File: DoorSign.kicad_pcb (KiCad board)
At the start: 2 copper layers, 37 parts, among them J1 Wall, J2 Taster, J3 Taster-LED, U1 Pico, U2 PC817, U3 LM2575-5.0BT

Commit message: Ignores
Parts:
- C1, C10: footprint Capacitor_THT:CP_Axial_L11.0mm_D8.0mm_P15.00mm_Horizontal -> Capacitor_THT:CP_Radial_D12.5mm_P5.00mm
- C3, C5, D3, D5: moved to B.Cu
- C6, C8, D6, D8: moved to F.Cu
- moved D8 183.1 mm to (50.5, 155.4)
- moved C8 166.6 mm to (60.1, 155.9), turned to -90 degrees
- moved C9 154.6 mm to (59.0, 141.6)
- moved D9 154.6 mm to (68.0, 141.0)
- moved D6 135.1 mm to (174.3, 166.4), turned to 0 degrees
- moved C6 134.6 mm to (164.0, 166.0)
- moved J1 121.1 mm to (162.0, 112.7)
- moved C10 115.9 mm to (182.0, 90.7)
- moved C2 113.5 mm to (56.5, 36.4)
- moved D2 113.5 mm to (65.0, 37.0)
- moved D3 113.4 mm to (65.5, 48.6), turned to 180 degrees
- moved C3 113.2 mm to (57.0, 49.0)
- moved D7 112.1 mm to (154.8, 149.0), turned to 90 degrees
- moved D12 104.6 mm to (161.9, 99.1)
- moved D13 104.6 mm to (154.7, 114.1)
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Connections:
- U1 pad 1: unconnected-(U1-Pad1) -> Net-(R4-Pad2)
- U1 pad 2: unconnected-(U1-Pad2) -> Net-(D2-Pad4)
- U1 pad 21: Net-(R4-Pad2) -> unconnected-(U1-Pad21)
- U1 pad 22: Net-(D2-Pad4) -> unconnected-(U1-Pad22)
- U1 pad 29: Net-(R1-Pad2) -> unconnected-(U1-Pad29)
- U1 pad 31: unconnected-(U1-Pad31) -> Net-(R1-Pad2)
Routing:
- net Net-(D7-Pad2): track 19.4 -> 167.5 mm, vias 0 -> 1
- net /8VAC-L: track 138.4 -> 268.8 mm
- net Net-(D3-Pad2): track 17.9 -> 141.9 mm, vias 0 -> 1
- net Net-(J1-Pad3): track 128.2 -> 229.9 mm, vias 0 -> 2
- net +3.3V: track 98.2 -> 198.1 mm
- net Net-(D2-Pad4): track 163.4 -> 80.0 mm, vias 0 -> 2
- net Net-(R1-Pad2): track 87.0 -> 161.5 mm
- net Net-(D6-Pad2): track 15.7 -> 56.7 mm, vias 0 -> 1
- net Net-(J3-Pad2): track 14.3 -> 47.9 mm
- net Net-(R4-Pad2): track 47.6 -> 76.6 mm
- net /8VAC-N: track 47.6 -> 24.6 mm
- net Net-(C10-Pad1): track 47.6 -> 30.7 mm
- net Net-(D8-Pad2): track 16.8 -> 28.6 mm, vias 0 -> 1
- net Net-(D10-Pad1): track 26.8 -> 16.7 mm
- net Net-(D11-Pad1): track 38.9 -> 29.0 mm
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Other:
- board outline added: 179.8 x 179.8 mm

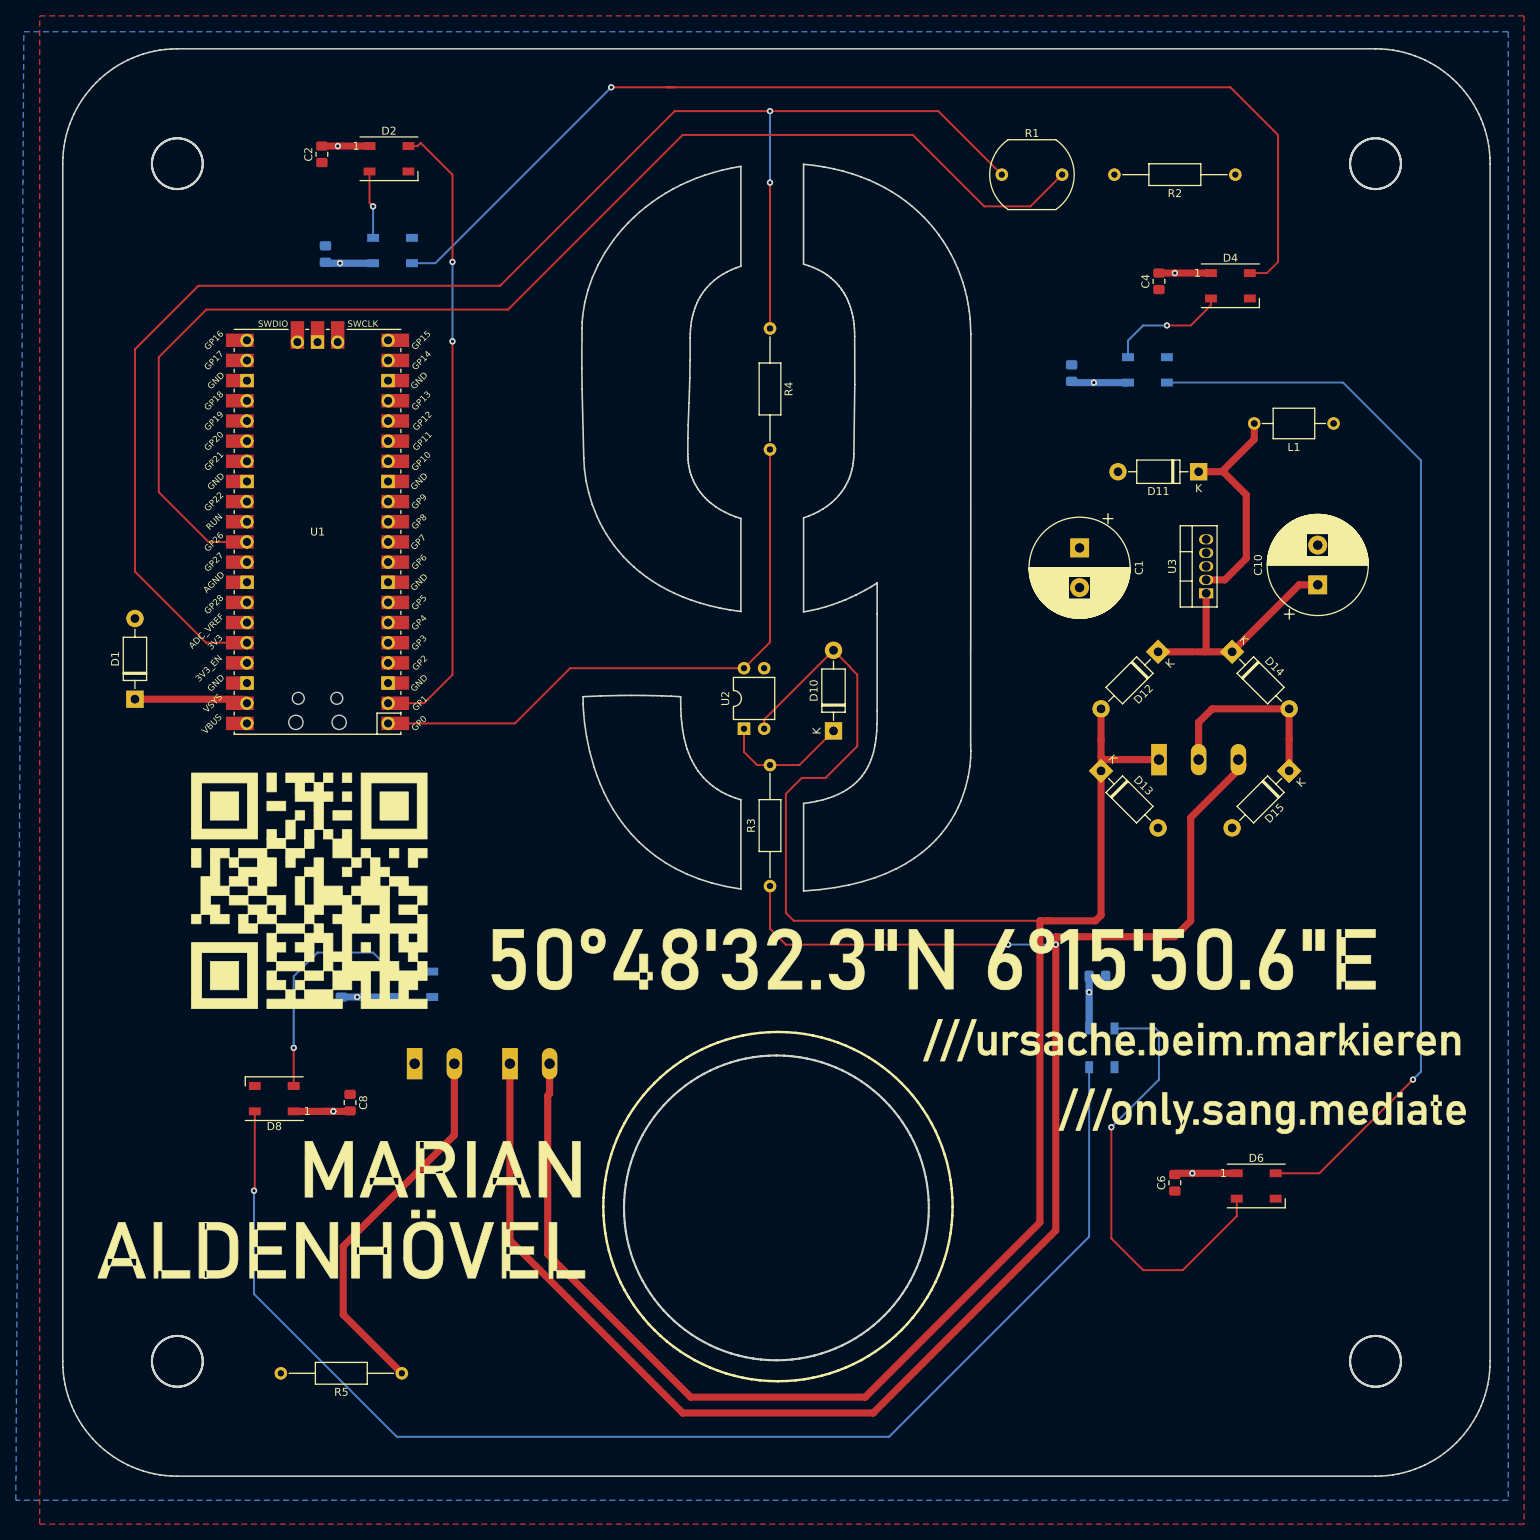
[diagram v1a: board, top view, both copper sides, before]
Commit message: Added BOM and partial schematics
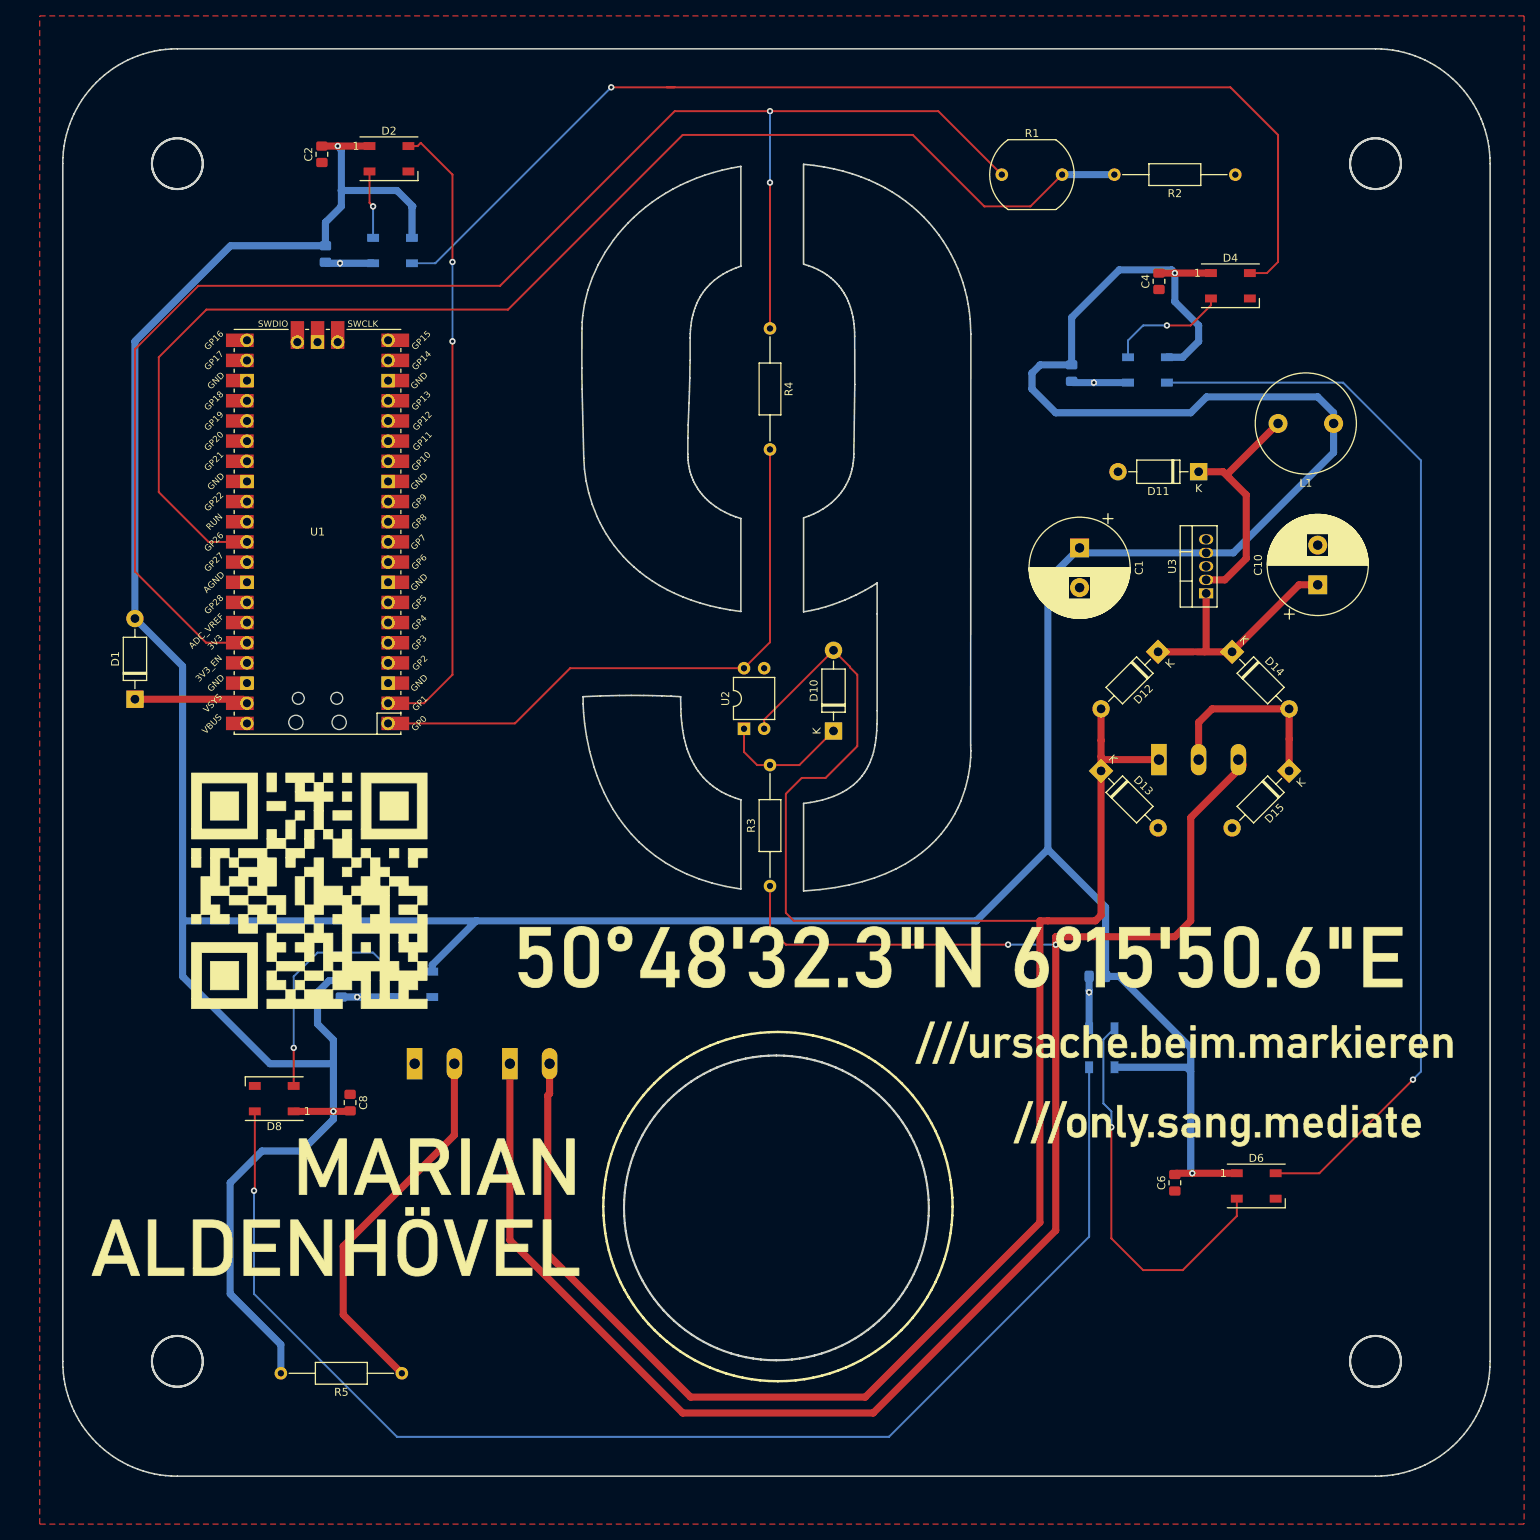
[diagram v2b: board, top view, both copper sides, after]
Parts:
- L1: value L -> 33uH; footprint Inductor_THT:L_Axial_L5.0mm_D3.6mm_P10.00mm_Horizontal_Murata_BL01RN1A2A2 -> Inductor_THT:L_Radial_D12.5mm_P7.00mm_Fastron_09HCP
- R2: value 100k -> 10k
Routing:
- net +5V: track 28.5 -> 600.7 mm
- net Net-(D6-Pad2): track 56.7 -> 49.9 mm
- net Net-(R1-Pad2): track 161.5 -> 168.1 mm
- net Net-(D11-Pad1): track 29.0 -> 30.8 mm
- removed copper zone on B.Cu, net +5V
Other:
- board text added: "<-- +5VDC Button Lamp"
- board text added: "<-- 8VAC L"
- board text added: "<-- 8VAC N"
- board text added: "<-- Button"
- board text added: "<-- GND Button Lamp"
- board text added: "<-- Ringer"

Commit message: added jumper for optocoupler
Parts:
- added JP4: Test, TestPoint:TestPoint_2Pads_Pitch2.54mm_Drill0.8mm, B.Cu at (97.0, 97.0)
- moved D1 5.53 mm to (35.0, 99.9), turned to -90 degrees
- moved C1 4.65 mm to (152.0, 90.7), turned to 90 degrees
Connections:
- C1 pad 1: +5V -> Net-(C1-Pad1)
- D1 pad 1: Net-(D1-Pad1) -> +5V
- D1 pad 2: +5V -> Net-(C1-Pad1)
- L1 pad 1: +5V -> Net-(C1-Pad1)
- U1 pad 39: Net-(D1-Pad1) -> +5V
- U3 pad 4: +5V -> Net-(C1-Pad1)
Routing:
- net Net-(C1-Pad1): track 0.00 -> 197.3 mm
- net Net-(D1-Pad1): track 14.3 -> 0.00 mm
- net +5V: track 600.7 -> 611.3 mm
- net Net-(JP4-Pad1): track 76.6 -> 80.9 mm
- net Net-(D5-Pad2): track 136.7 -> 138.4 mm

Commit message: connected all GND pins on the Pico
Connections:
- U1 pad 13: unconnected-(U1-Pad13) -> GND
- U1 pad 18: unconnected-(U1-Pad18) -> GND
- U1 pad 23: unconnected-(U1-Pad23) -> GND
- U1 pad 28: unconnected-(U1-Pad28) -> GND
- U1 pad 3: unconnected-(U1-Pad3) -> GND
- U1 pad 42: unconnected-(U1-Pad42) -> GND
- U1 pad 8: unconnected-(U1-Pad8) -> GND

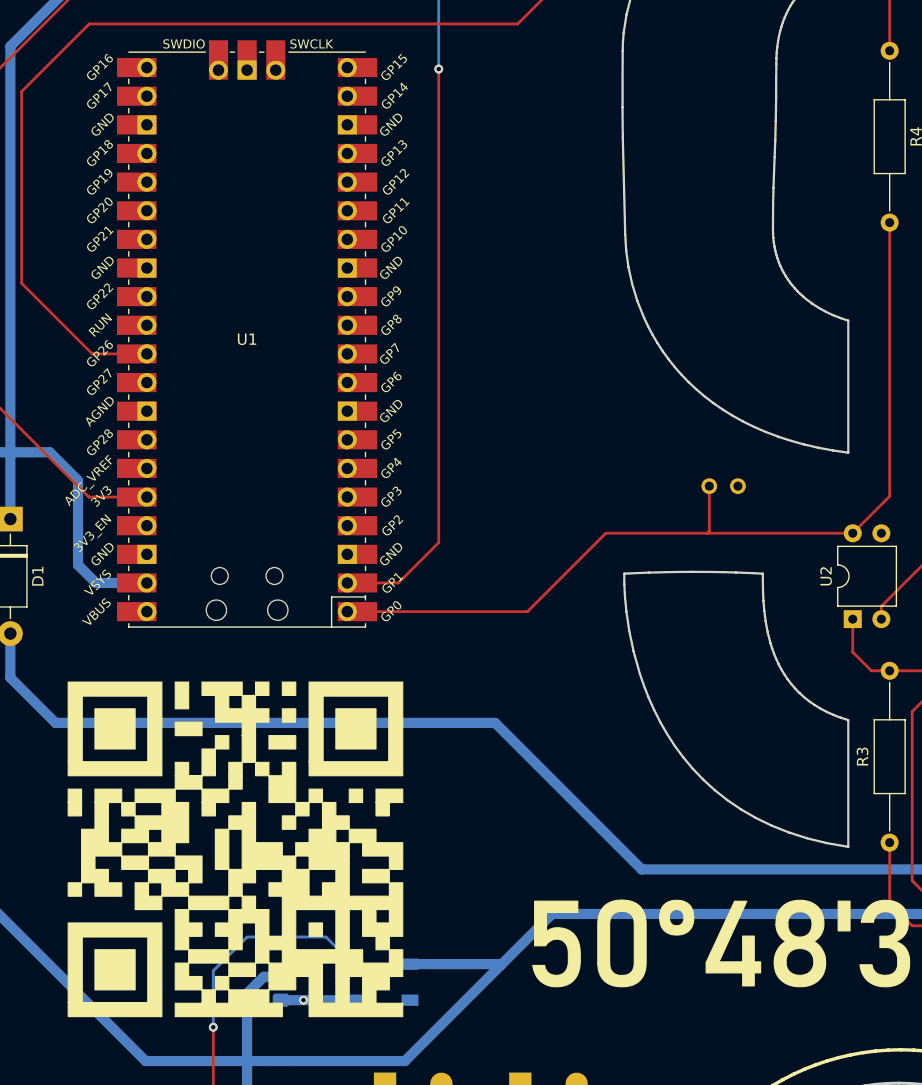
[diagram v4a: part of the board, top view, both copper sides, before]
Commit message: Rewired GPIOs for compatibility with Raspberry Pi Pico W
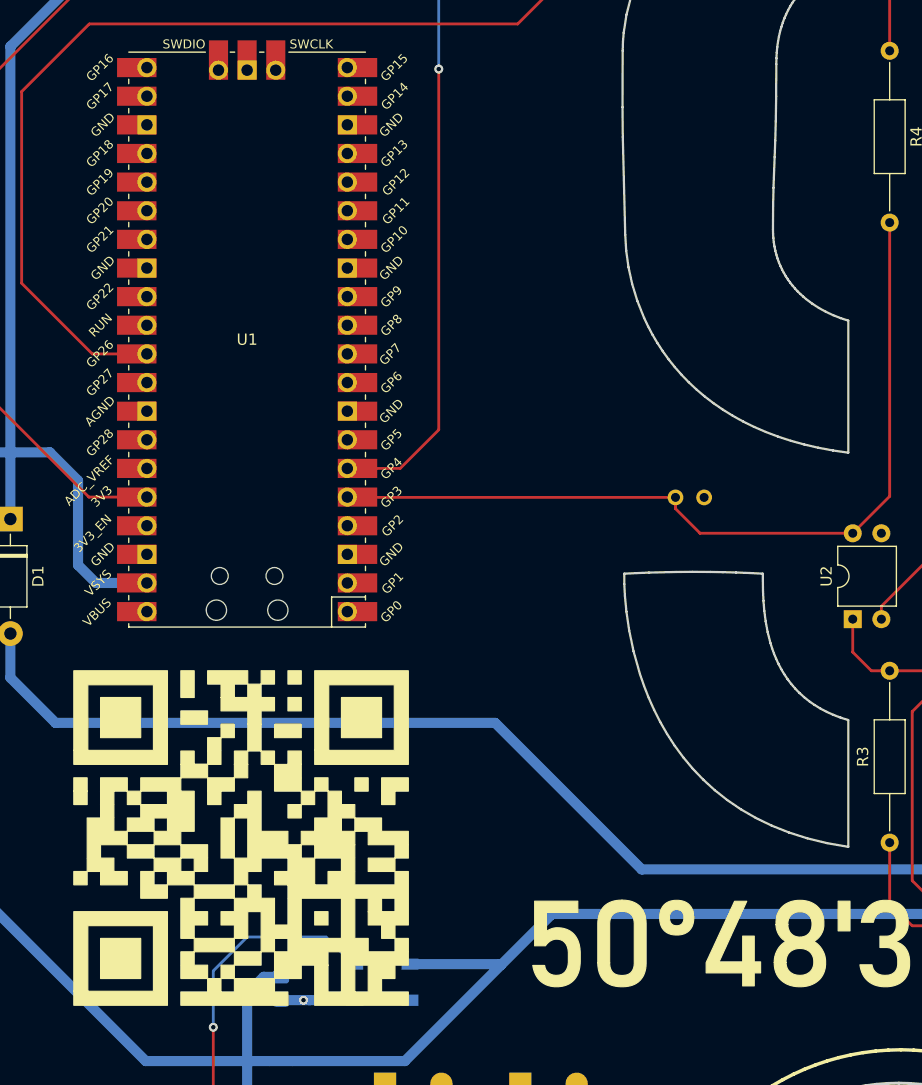
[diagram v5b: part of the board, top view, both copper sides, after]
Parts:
- moved JP4 3.16 mm to (94.0, 98.0)
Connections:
- U1 pad 1: Net-(JP4-Pad1) -> unconnected-(U1-Pad1)
- U1 pad 2: Net-(D2-Pad4) -> unconnected-(U1-Pad2)
- U1 pad 5: unconnected-(U1-Pad5) -> Net-(JP4-Pad1)
- U1 pad 6: unconnected-(U1-Pad6) -> Net-(D2-Pad4)
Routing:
- net Net-(D2-Pad4): track 79.6 -> 69.6 mm
- net Net-(JP4-Pad1): track 80.9 -> 75.7 mm
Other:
- board text added: "Test"
